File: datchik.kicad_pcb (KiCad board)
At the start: 2 copper layers, 2 parts, among them P1 CONN_5

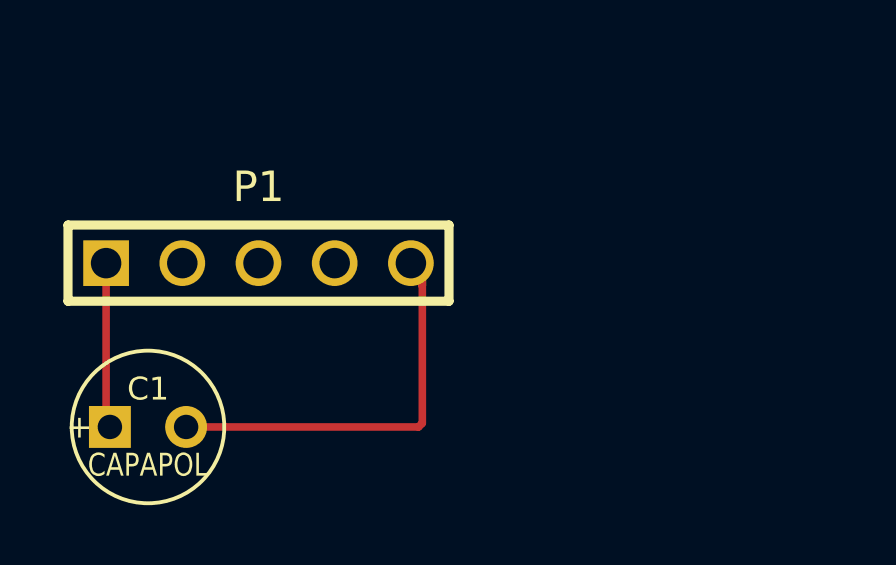
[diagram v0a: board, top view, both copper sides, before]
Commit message: добавлен кварц и кондеры
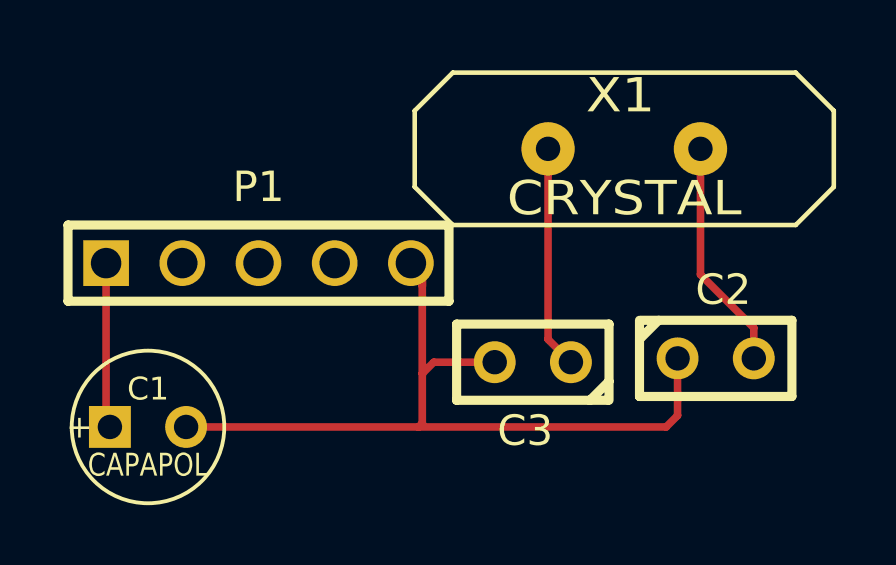
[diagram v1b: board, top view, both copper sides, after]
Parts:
- added C2: C, C1, F.Cu at (40.5, 32.0)
- added C3: C, C1, F.Cu at (34.4, 32.1)
- added X1: CRYSTAL, HC-18UV, F.Cu at (37.5, 25.0)
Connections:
- net /GND renamed GND
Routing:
- net GND: track 14.1 -> 27.3 mm
- net /XTL1: track 0.00 -> 7.72 mm
- net /XTL2: track 0.00 -> 7.43 mm
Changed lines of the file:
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@@
 (kicad_pcb (version 3) (host pcbnew "(2013-07-07 BZR 4022)-stable")
   (general
-    (links 2)
+    (links 6)
     (no_connects 0)
-    (area 15.901999 18.441999 51.027001 39.597001)
+    (area 0 0 0 0)
     (thickness 1.6)
     (drawings 5)
-    (tracks 8)
+    (tracks 19)
     (zones 0)
-    (modules 2)
-    (nets 3)
+    (modules 5)
+    (nets 5)
   )
   (page A3)
@@
   )
   (net 0 "")
-  (net 1 /GND)
-  (net 2 /VCC)
+  (net 1 /VCC)
+  (net 2 /XTL1)
+  (net 3 /XTL2)
+  (net 4 GND)
   (net_class Default "Это класс цепей по умолчанию."
     (clearance 0.254)
@@
     (uvia_drill 0.127)
     (add_net "")
-    (add_net /GND)
     (add_net /VCC)
+    (add_net /XTL1)
+    (add_net /XTL2)
+    (add_net GND)
   )
   (module PIN_ARRAY_5x1 (layer F.Cu)
@@
     (pad 1 thru_hole rect (at -5.08 0) (size 1.524 1.524) (drill 1.016)
       (layers *.Cu *.Mask F.SilkS)
-      (net 2 /VCC)
+      (net 1 /VCC)
     )
     (pad 2 thru_hole circle (at -2.54 0) (size 1.524 1.524) (drill 1.016)
@@
     (pad 5 thru_hole circle (at 5.08 0) (size 1.524 1.524) (drill 1.016)
       (layers *.Cu *.Mask F.SilkS)
-      (net 1 /GND)
+      (net 4 GND)
     )
     (model pin_array/pins_array_5x1.wrl
@@
     (pad 1 thru_hole rect (at -1.27 0) (size 1.397 1.397) (drill 0.8128)
       (layers *.Cu *.Mask F.SilkS)
-      (net 2 /VCC)
+      (net 1 /VCC)
     )
     (pad 2 thru_hole circle (at 1.27 0) (size 1.397 1.397) (drill 0.8128)
       (layers *.Cu *.Mask F.SilkS)
-      (net 1 /GND)
+      (net 4 GND)
     )
     (model discret/c_vert_c1v5.wrl
+      (at (xyz 0 0 0))
+      (scale (xyz 1 1 1))
+      (rotate (xyz 0 0 0))
+    )
+  )
+  (module HC-18UV (layer F.Cu)
+    (at 37.465 25.019)
+    (descr "Quartz boitier HC-18U vertical")
+    (tags "QUARTZ DEV")
+    (autoplace_cost180 10)
+    (fp_text reference X1 (at -0.127 -1.778) (layer F.SilkS)
+      (effects (font (size 1.143 1.27) (thickness 0.1524)))
+    )
+    (fp_text value CRYSTAL (at 0 1.651) (layer F.SilkS)
+      (effects (font (size 1.143 1.27) (thickness 0.1524)))
+    )
+    (fp_line (start -6.985 -1.27) (end -5.715 -2.54) (layer F.SilkS) (width 0.1524))
+    (fp_line (start 5.715 -2.54) (end 6.985 -1.27) (layer F.SilkS) (width 0.1524))
+    (fp_line (start 6.985 1.27) (end 5.715 2.54) (layer F.SilkS) (width 0.1524))
+    (fp_line (start -6.985 1.27) (end -5.715 2.54) (layer F.SilkS) (width 0.1524))
+    (fp_line (start -5.715 -2.54) (end 5.715 -2.54) (layer F.SilkS) (width 0.1524))
+    (fp_line (start -6.985 -1.27) (end -6.985 1.27) (layer F.SilkS) (width 0.1524))
+    (fp_line (start -5.715 2.54) (end 5.715 2.54) (layer F.SilkS) (width 0.1524))
+    (fp_line (start 6.985 1.27) (end 6.985 -1.27) (layer F.SilkS) (width 0.1524))
+    (pad 1 thru_hole circle (at -2.54 0) (size 1.778 1.778) (drill 0.8128)
+      (layers *.Cu *.Mask F.SilkS)
+      (net 3 /XTL2)
+    )
+    (pad 2 thru_hole circle (at 2.54 0) (size 1.778 1.778) (drill 0.8128)
+      (layers *.Cu *.Mask F.SilkS)
+      (net 2 /XTL1)
+    )
+    (model discret/crystal_hc18u_vertical.wrl
+      (at (xyz 0 0 0))
+      (scale (xyz 1 1 1))
+      (rotate (xyz 0 0 0))
+    )
+    (model discret/xtal/crystal_hc18u_vertical.wrl
+      (at (xyz 0 0 0))
+      (scale (xyz 1 1 1))
+      (rotate (xyz 0 0 0))
+    )
+  )
+  (module C1 (layer F.Cu)
+    (at 40.513 32.004)
+    (descr "Condensateur e = 1 pas")
+    (tags C)
+    (fp_text reference C2 (at 0.254 -2.286) (layer F.SilkS)
+      (effects (font (size 1.016 1.016) (thickness 0.2032)))
+    )
+    (fp_text value C (at 0 -2.286) (layer F.SilkS) hide
+      (effects (font (size 1.016 1.016) (thickness 0.2032)))
+    )
+    (fp_line (start -2.4892 -1.27) (end 2.54 -1.27) (layer F.SilkS) (width 0.3048))
+    (fp_line (start 2.54 -1.27) (end 2.54 1.27) (layer F.SilkS) (width 0.3048))
+    (fp_line (start 2.54 1.27) (end -2.54 1.27) (layer F.SilkS) (width 0.3048))
+    (fp_line (start -2.54 1.27) (end -2.54 -1.27) (layer F.SilkS) (width 0.3048))
+    (fp_line (start -2.54 -0.635) (end -1.905 -1.27) (layer F.SilkS) (width 0.3048))
+    (pad 1 thru_hole circle (at -1.27 0) (size 1.397 1.397) (drill 0.8128)
+      (layers *.Cu *.Mask F.SilkS)
+      (net 4 GND)
+    )
+    (pad 2 thru_hole circle (at 1.27 0) (size 1.397 1.397) (drill 0.8128)
+      (layers *.Cu *.Mask F.SilkS)
+      (net 2 /XTL1)
+    )
+    (model discret/capa_1_pas.wrl
+      (at (xyz 0 0 0))
+      (scale (xyz 1 1 1))
+      (rotate (xyz 0 0 0))
+    )
+  )
+  (module C1 (layer F.Cu)
+    (at 34.417 32.131 180)
+    (descr "Condensateur e = 1 pas")
+    (tags C)
+    (fp_text reference C3 (at 0.254 -2.286 180) (layer F.SilkS)
+      (effects (font (size 1.016 1.016) (thickness 0.2032)))
+    )
+    (fp_text value C (at 0 -2.286 180) (layer F.SilkS) hide
+      (effects (font (size 1.016 1.016) (thickness 0.2032)))
+    )
+    (fp_line (start -2.4892 -1.27) (end 2.54 -1.27) (layer F.SilkS) (width 0.3048))
+    (fp_line (start 2.54 -1.27) (end 2.54 1.27) (layer F.SilkS) (width 0.3048))
+    (fp_line (start 2.54 1.27) (end -2.54 1.27) (layer F.SilkS) (width 0.3048))
+    (fp_line (start -2.54 1.27) (end -2.54 -1.27) (layer F.SilkS) (width 0.3048))
+    (fp_line (start -2.54 -0.635) (end -1.905 -1.27) (layer F.SilkS) (width 0.3048))
+    (pad 1 thru_hole circle (at -1.27 0 180) (size 1.397 1.397) (drill 0.8128)
+      (layers *.Cu *.Mask F.SilkS)
+      (net 3 /XTL2)
+    )
+    (pad 2 thru_hole circle (at 1.27 0 180) (size 1.397 1.397) (drill 0.8128)
+      (layers *.Cu *.Mask F.SilkS)
+      (net 4 GND)
+    )
+    (model discret/capa_1_pas.wrl
       (at (xyz 0 0 0))
       (scale (xyz 1 1 1))
@@
   (gr_line (start 16.002 39.497) (end 50.927 39.497) (angle 90) (layer Eco2.User) (width 0.2))
   (gr_line (start 16.002 18.542) (end 16.002 39.497) (angle 90) (layer Eco2.User) (width 0.2))
-  (segment (start 30.734 29.591) (end 30.734 29.21) (width 0.254) (layer F.Cu) (net 1))
-  (segment (start 30.734 29.21) (end 30.353 28.829) (width 0.254) (layer F.Cu) (net 1))
-  (segment (start 22.86 34.29) (end 30.607 34.29) (width 0.254) (layer F.Cu) (net 1))
-  (segment (start 30.734 34.163) (end 30.734 29.591) (width 0.254) (layer F.Cu) (net 1))
-  (segment (start 30.734 29.591) (end 30.734 28.956) (width 0.254) (layer F.Cu) (net 1))
-  (segment (start 30.607 34.29) (end 30.734 34.163) (width 0.254) (layer F.Cu) (net 1))
-  (segment (start 20.193 28.829) (end 20.193 34.163) (width 0.254) (layer F.Cu) (net 2))
-  (segment (start 20.193 34.163) (end 20.32 34.29) (width 0.254) (layer F.Cu) (net 2))
+  (segment (start 20.193 28.829) (end 20.193 34.163) (width 0.254) (layer F.Cu) (net 1))
+  (segment (start 20.193 34.163) (end 20.32 34.29) (width 0.254) (layer F.Cu) (net 1))
+  (segment (start 40.005 25.019) (end 40.005 29.21) (width 0.254) (layer F.Cu) (net 2) (status 400000))
+  (segment (start 41.783 30.988) (end 41.783 32.004) (width 0.254) (layer F.Cu) (net 2) (status 800000))
+  (segment (start 40.005 29.21) (end 41.783 30.988) (width 0.254) (layer F.Cu) (net 2))
+  (segment (start 34.925 25.019) (end 34.925 31.369) (width 0.254) (layer F.Cu) (net 3) (status 400000))
+  (segment (start 34.925 31.369) (end 35.687 32.131) (width 0.254) (layer F.Cu) (net 3) (status 800000))
+  (segment (start 39.243 32.004) (end 39.243 33.909) (width 0.254) (layer F.Cu) (net 4) (status 400000))
+  (segment (start 38.862 34.29) (end 30.607 34.29) (width 0.254) (layer F.Cu) (net 4))
+  (segment (start 39.243 33.909) (end 38.862 34.29) (width 0.254) (layer F.Cu) (net 4))
+  (segment (start 33.147 32.131) (end 31.115 32.131) (width 0.254) (layer F.Cu) (net 4) (status 400000))
+  (segment (start 31.115 32.131) (end 30.734 32.512) (width 0.254) (layer F.Cu) (net 4))
+  (segment (start 30.734 29.591) (end 30.734 29.21) (width 0.254) (layer F.Cu) (net 4))
+  (segment (start 30.734 29.21) (end 30.353 28.829) (width 0.254) (layer F.Cu) (net 4))
+  (segment (start 22.86 34.29) (end 30.607 34.29) (width 0.254) (layer F.Cu) (net 4))
+  (segment (start 30.734 34.163) (end 30.734 32.512) (width 0.254) (layer F.Cu) (net 4))
+  (segment (start 30.734 32.512) (end 30.734 29.591) (width 0.254) (layer F.Cu) (net 4))
+  (segment (start 30.734 29.591) (end 30.734 28.956) (width 0.254) (layer F.Cu) (net 4))
+  (segment (start 30.607 34.29) (end 30.734 34.163) (width 0.254) (layer F.Cu) (net 4))
 )
